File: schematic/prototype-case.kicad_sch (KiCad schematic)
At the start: 11 parts, among them J1 NMJ6HF-S, J2 NMJ6HF-S, J3 STRIP 4-WAY (IN THE CASE), J4 CODEC HEADER (TODAY), J5 NMJ6HF-S

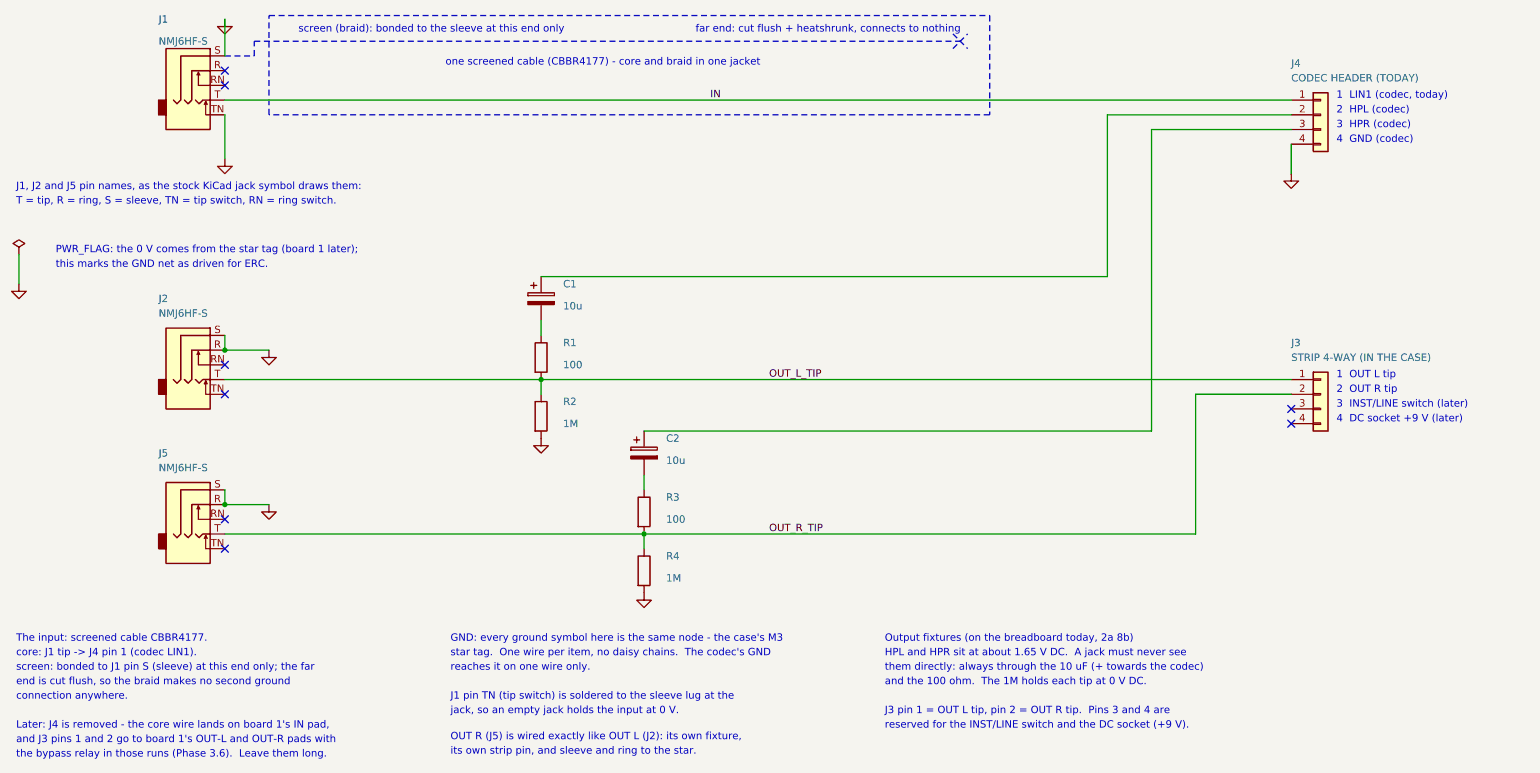
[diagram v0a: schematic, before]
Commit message: schematic, docs: the NMJ6HF-S has six lugs, not five
Neutrik's documentation for the jack says three switching contacts, and their
Jacks-Circuits chart puts the part in "3x switching (normalling) Stereo
N*J6**": tip, ring and sleeve each carry a switch, so there are six lugs in two
rows, each switch directly opposite its contact and closed while no plug is
inserted. Their footprints agree — pads T/R/S in one row, TN/RN/SN in the other.

The sheet now uses KiCad's six-lug symbol (AudioJack3_Switch). S moves 2.54 mm
up and SN takes its old place, which also removed the sleeve-to-ring link at the
output jacks: those two lugs now reach the star on their own wires, as
build-board1.md always said. Stage 2's meter check asks for all six.
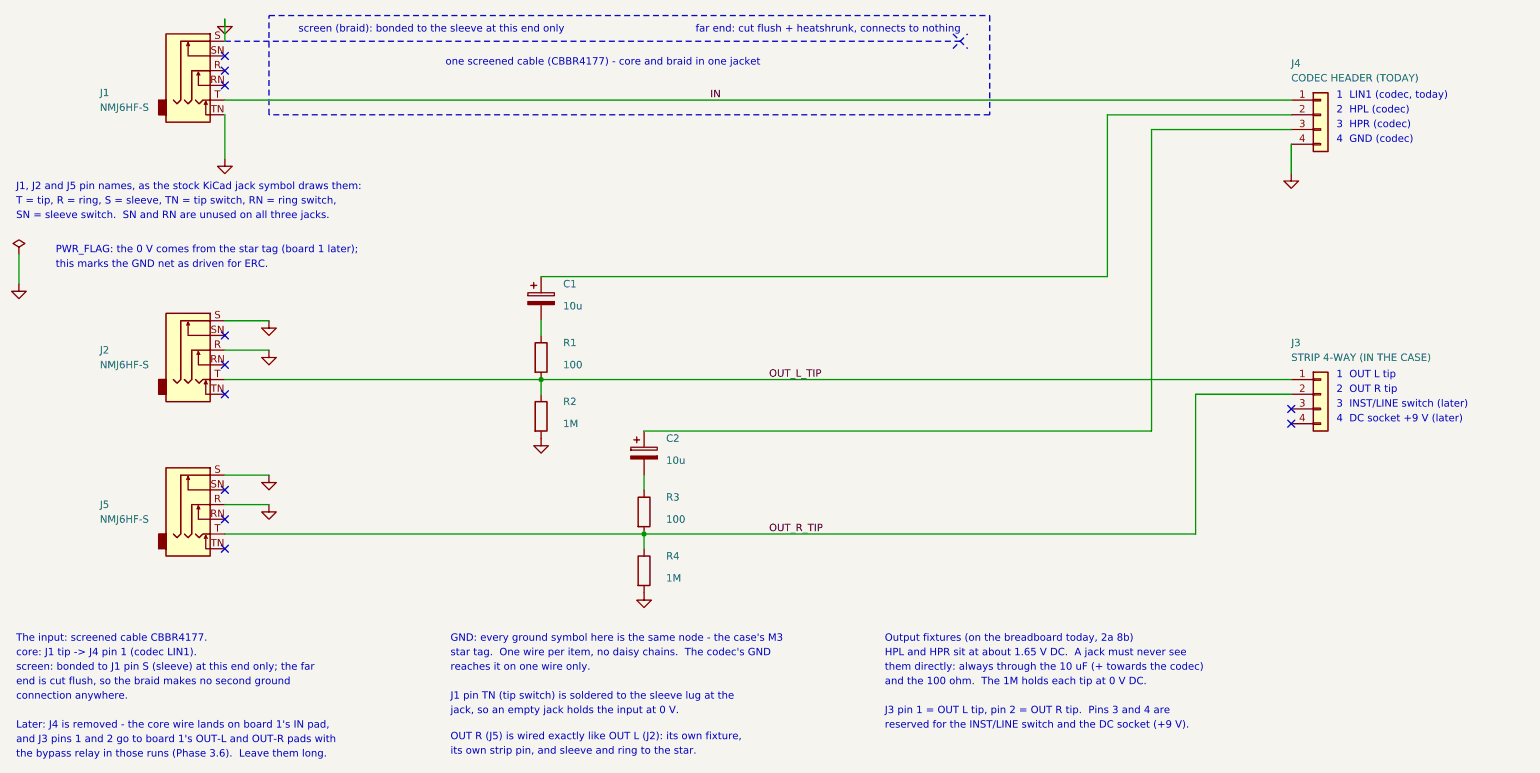
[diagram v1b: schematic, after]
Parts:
- removed J1, J2, J5: NMJ6HF-S, symbol Connector_Audio:AudioJack3_SwitchTR
- removed J3: STRIP 4-WAY (IN THE CASE), symbol Connector_Generic:Conn_01x04
- added J1, J2, J5: NMJ6HF-S, symbol Connector_Audio:AudioJack3_Switch
- added J4: CODEC HEADER (TODAY), symbol Connector_Generic:Conn_01x04
- J3: renamed from J4; value CODEC HEADER (TODAY) -> STRIP 4-WAY (IN THE CASE)
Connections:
- net GND: now also J1.S, J1.TN, J2.R, J2.S, J4.4 (Pin_4), J5.R, J5.S; no longer J3.4 (Pin_4)
- net IN: now also J1.T, J4.1 (Pin_1); no longer J3.1 (Pin_1)
- net OUT_L_TIP: now also J3.1 (Pin_1), J2.T
- net OUT_R_TIP: now also J3.2 (Pin_2), J5.T
- net at C1.1: now also J4.2 (Pin_2); no longer J3.2 (Pin_2)
- net at J3.3 (Pin_3): no longer C2.1
- new net: C2.1, J4.3 (Pin_3)
- no-connect marks 8 -> 11
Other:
- note added: "SN = sleeve switch. SN and RN are unused on all three jacks."
- note added: "T = tip, R = ring, S = sleeve, TN = tip switch, RN = ring switch,"
- note removed: "T = tip, R = ring, S = sleeve, TN = tip switch, RN = ring switch."
- moved on the sheet: J3
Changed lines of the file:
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@@
 	(polyline
 		(pts
-			(xy 66.04 54.61) (xy 71.12 54.61) (xy 71.12 52.07) (xy 193.04 52.07)
+			(xy 66.04 52.07) (xy 193.04 52.07)
 		)
 		(stroke
@@
 			(type none)
 		)
-	)
-	(junction
-		(at 66.04 105.41)
-		(diameter 0)
-		(color 0 0 0 0)
-	)
-	(junction
-		(at 66.04 132.08)
-		(diameter 0)
-		(color 0 0 0 0)
 	)
 	(junction
@@
 	)
 	(no_connect
+		(at 66.04 54.61)
+	)
+	(no_connect
 		(at 66.04 107.95)
 	)
@@
 	)
 	(no_connect
+		(at 66.04 102.87)
+	)
+	(no_connect
 		(at 66.04 134.62)
 	)
@@
 	)
 	(no_connect
+		(at 66.04 129.54)
+	)
+	(no_connect
 		(at 250.19 115.57)
 	)
@@
 	(wire
 		(pts
-			(xy 66.04 48.26) (xy 66.04 54.61)
+			(xy 66.04 48.26) (xy 66.04 52.07)
 		)
 		(stroke
@@
 	(wire
 		(pts
-			(xy 66.04 102.87) (xy 66.04 105.41)
+			(xy 66.04 100.33) (xy 73.66 100.33)
 		)
 		(stroke
@@
 	(wire
 		(pts
-			(xy 66.04 129.54) (xy 66.04 132.08)
+			(xy 66.04 127.0) (xy 73.66 127.0)
 		)
 		(stroke
@@
 		)
 	)
-	(text "T = tip, R = ring, S = sleeve, TN = tip switch, RN = ring switch."
+	(text "T = tip, R = ring, S = sleeve, TN = tip switch, RN = ring switch,"
 		(exclude_from_sim no)
 		(at 30 80.5 0)
+		(effects
+			(font
+				(size 1.27 1.27)
+			)
+			(justify left bottom)
+		)
+	)
+	(text "SN = sleeve switch.  SN and RN are unused on all three jacks."
+		(exclude_from_sim no)
+		(at 30 83 0)
 		(effects
 			(font
@@
 	)
 	(symbol
-		(lib_id "Connector_Audio:AudioJack3_SwitchTR")
+		(lib_id "Connector_Audio:AudioJack3_Switch")
 		(at 60.96 57.15 0)
 		(unit 1)
@@
 		(dnp no)
 		(property "Reference" "J1"
-			(at 54.61 48.26 0)
+			(at 44.45 60.96 0)
 			(effects
 				(font
@@
 		)
 		(property "Value" "NMJ6HF-S"
-			(at 54.61 52.07 0)
+			(at 44.45 63.5 0)
 			(effects
 				(font
@@
 		)
 		(pin "S"
+		)
+		(pin "SN"
 		)
 		(pin "T"
@@
 	)
 	(symbol
-		(lib_id "Connector_Audio:AudioJack3_SwitchTR")
+		(lib_id "Connector_Audio:AudioJack3_Switch")
 		(at 60.96 105.41 0)
 		(unit 1)
@@
 		(dnp no)
 		(property "Reference" "J2"
-			(at 54.61 96.52 0)
+			(at 44.45 105.41 0)
 			(effects
 				(font
@@
 		)
 		(property "Value" "NMJ6HF-S"
-			(at 54.61 99.06 0)
+			(at 44.45 107.95 0)
 			(effects
 				(font
@@
 		)
 		(pin "S"
+		)
+		(pin "SN"
 		)
 		(pin "T"
@@
 	)
 	(symbol
-		(lib_id "Connector_Audio:AudioJack3_SwitchTR")
+		(lib_id "Connector_Audio:AudioJack3_Switch")
 		(at 60.96 132.08 0)
 		(unit 1)
@@
 		(dnp no)
 		(property "Reference" "J5"
-			(at 54.61 123.19 0)
+			(at 44.45 132.08 0)
 			(effects
 				(font
@@
 		)
 		(property "Value" "NMJ6HF-S"
-			(at 54.61 125.73 0)
+			(at 44.45 134.62 0)
 			(effects
 				(font
@@
 		)
 		(pin "S"
+		)
+		(pin "SN"
 		)
 		(pin "T"
@@
 					(unit 1)
 				)
+			)
+		)
+	)
+	(symbol
+		(lib_id "power:GND")
+		(at 73.66 100.33 0)
+		(unit 1)
+		(exclude_from_sim no)
+		(in_bom yes)
+		(on_board yes)
+		(dnp no)
+		(property "Reference" "#PWR09"
+			(at 69.0 96.52 0)
+			(effects
+				(font
+					(size 1.27 1.27)
+				)
+				(justify left)
+				(hide yes)
+			)
+		)
+		(property "Value" "GND"
+			(at 69.0 103.3 0)
+			(effects
+				(font
+					(size 1.27 1.27)
+				)
+				(justify left)
+				(hide yes)
+			)
+		)
+		(property "Footprint" ""
+			(at 73.66 100.33 0)
+			(effects
+				(font
+					(size 1.27 1.27)
+				)
+				(hide yes)
+			)
+		)
+		(property "Datasheet" ""
+			(at 73.66 100.33 0)
+			(effects
+				(font
+					(size 1.27 1.27)
+				)
+				(hide yes)
+			)
+		)
+		(property "Description" ""
+			(at 73.66 100.33 0)
+			(effects
+				(font
+					(size 1.27 1.27)
+				)
+				(hide yes)
+			)
+		)
+		(pin "1"
+		)
+		(instances
+			(project "case-wiring"
+				(path "/6df129cb-54f5-5f8a-bfab-1519d9f2e8e7"
+					(reference "#PWR09")
+					(unit 1)
+				)
+			)
+		)
+	)
+	(symbol
+		(lib_id "power:GND")
+		(at 73.66 127.0 0)
+		(unit 1)
+		(exclude_from_sim no)
+		(in_bom yes)
+		(on_board yes)
+		(dnp no)
+		(property "Reference" "#PWR10"
+			(at 69.0 123.19 0)
+			(effects
+				(font
+					(size 1.27 1.27)
+				)
+				(justify left)
+				(hide yes)
+			)
+		)
+		(property "Value" "GND"
+			(at 69.0 130.0 0)
+			(effects
+				(font
+					(size 1.27 1.27)
+				)
+				(justify left)
+				(hide yes)
+			)
+		)
+		(property "Footprint" ""
+			(at 73.66 127.0 0)
+			(effects
+				(font
+					(size 1.27 1.27)
+				)
+				(hide yes)
+			)
+		)
+		(property "Datasheet" ""
+			(at 73.66 127.0 0)
+			(effects
+				(font
+					(size 1.27 1.27)
+				)
+				(hide yes)
+			)
+		)
+		(property "Description" ""
+			(at 73.66 127.0 0)
+			(effects
+				(font
+					(size 1.27 1.27)
+				)
+				(hide yes)
+			)
+		)
+		(pin "1"
+		)
+		(instances
+			(project "case-wiring"
+				(path "/6df129cb-54f5-5f8a-bfab-1519d9f2e8e7"
+					(reference "#PWR10")
+					(unit 1)
+				)
